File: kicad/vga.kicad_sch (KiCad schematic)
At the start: 5 parts, among them J10 DE15, U20 XC95108PC84

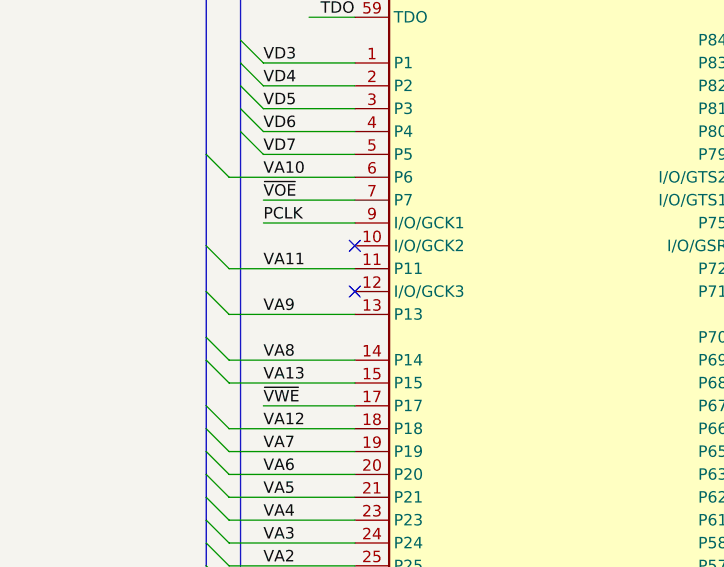
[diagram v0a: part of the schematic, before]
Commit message: hw: add missing shload_n connection
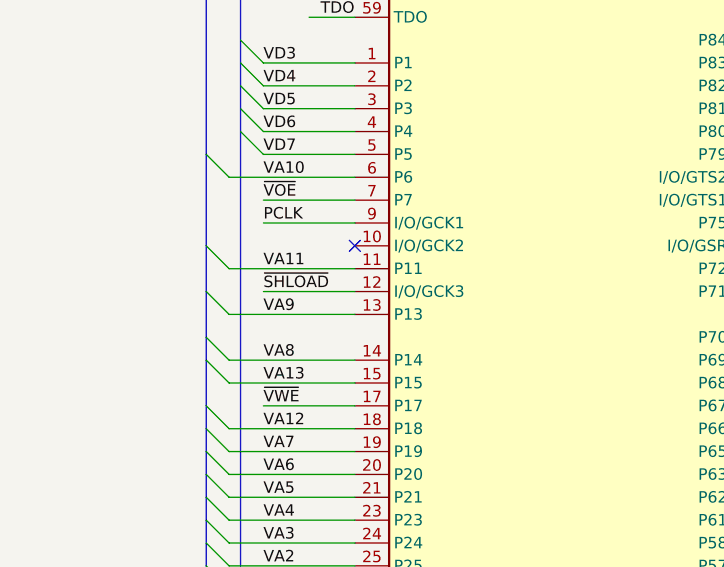
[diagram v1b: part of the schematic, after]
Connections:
- net ~{SHLOAD}: now also U20.12 (I/O/GCK3)
- no-connect marks 11 -> 10
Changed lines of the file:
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@@
 		(title "VGA")
 		(date "2025-06-18")
-		(rev "A")
+		(rev "B")
 		(company "A.K.")
 	)
@@
 	)
 	(no_connect
-		(at 102.87 102.87)
-	)
-	(no_connect
 		(at 250.19 85.09)
 	)
@@
 		(pts
 			(xy 123.19 58.42) (xy 120.65 58.42)
+		)
+		(stroke
+			(width 0)
+			(type default)
+		)
+	)
+	(wire
+		(pts
+			(xy 92.71 102.87) (xy 102.87 102.87)
 		)
 		(stroke
@@
 		)
 	)
+	(label "~{SHLOAD}"
+		(at 92.71 102.87 0)
+		(effects
+			(font
+				(size 1.27 1.27)
+			)
+			(justify left bottom)
+		)
+	)

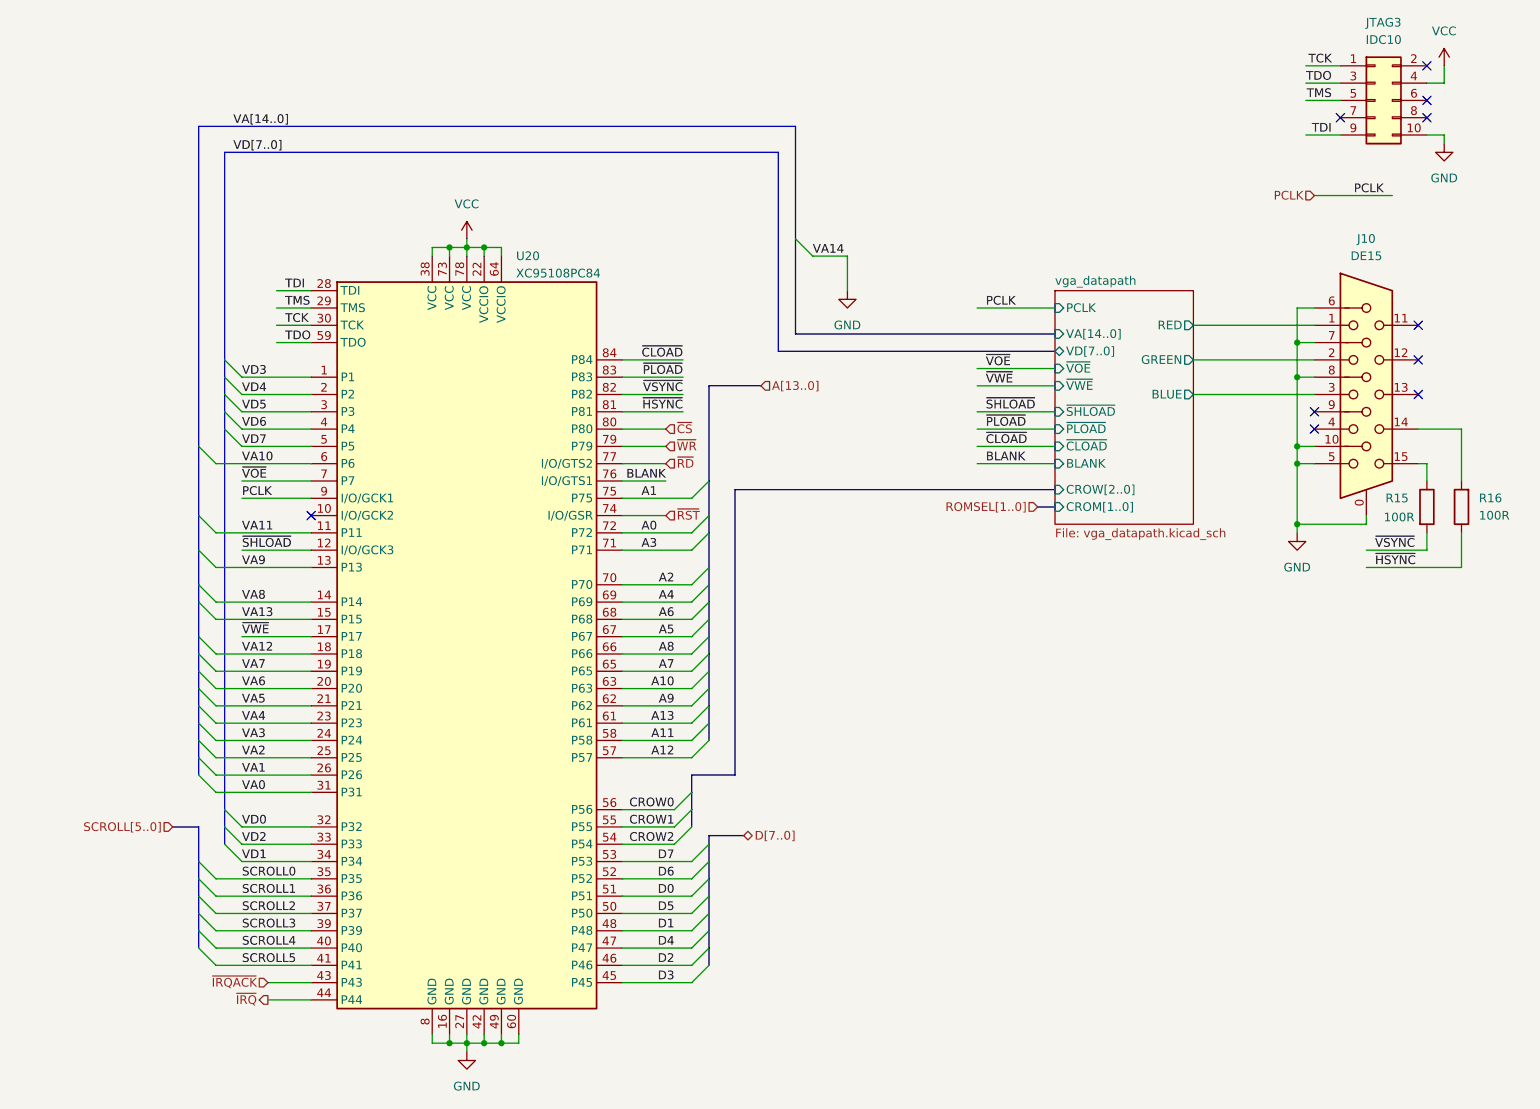
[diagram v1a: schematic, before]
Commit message: hw: replace CPLD JTAG connector, minor fixes
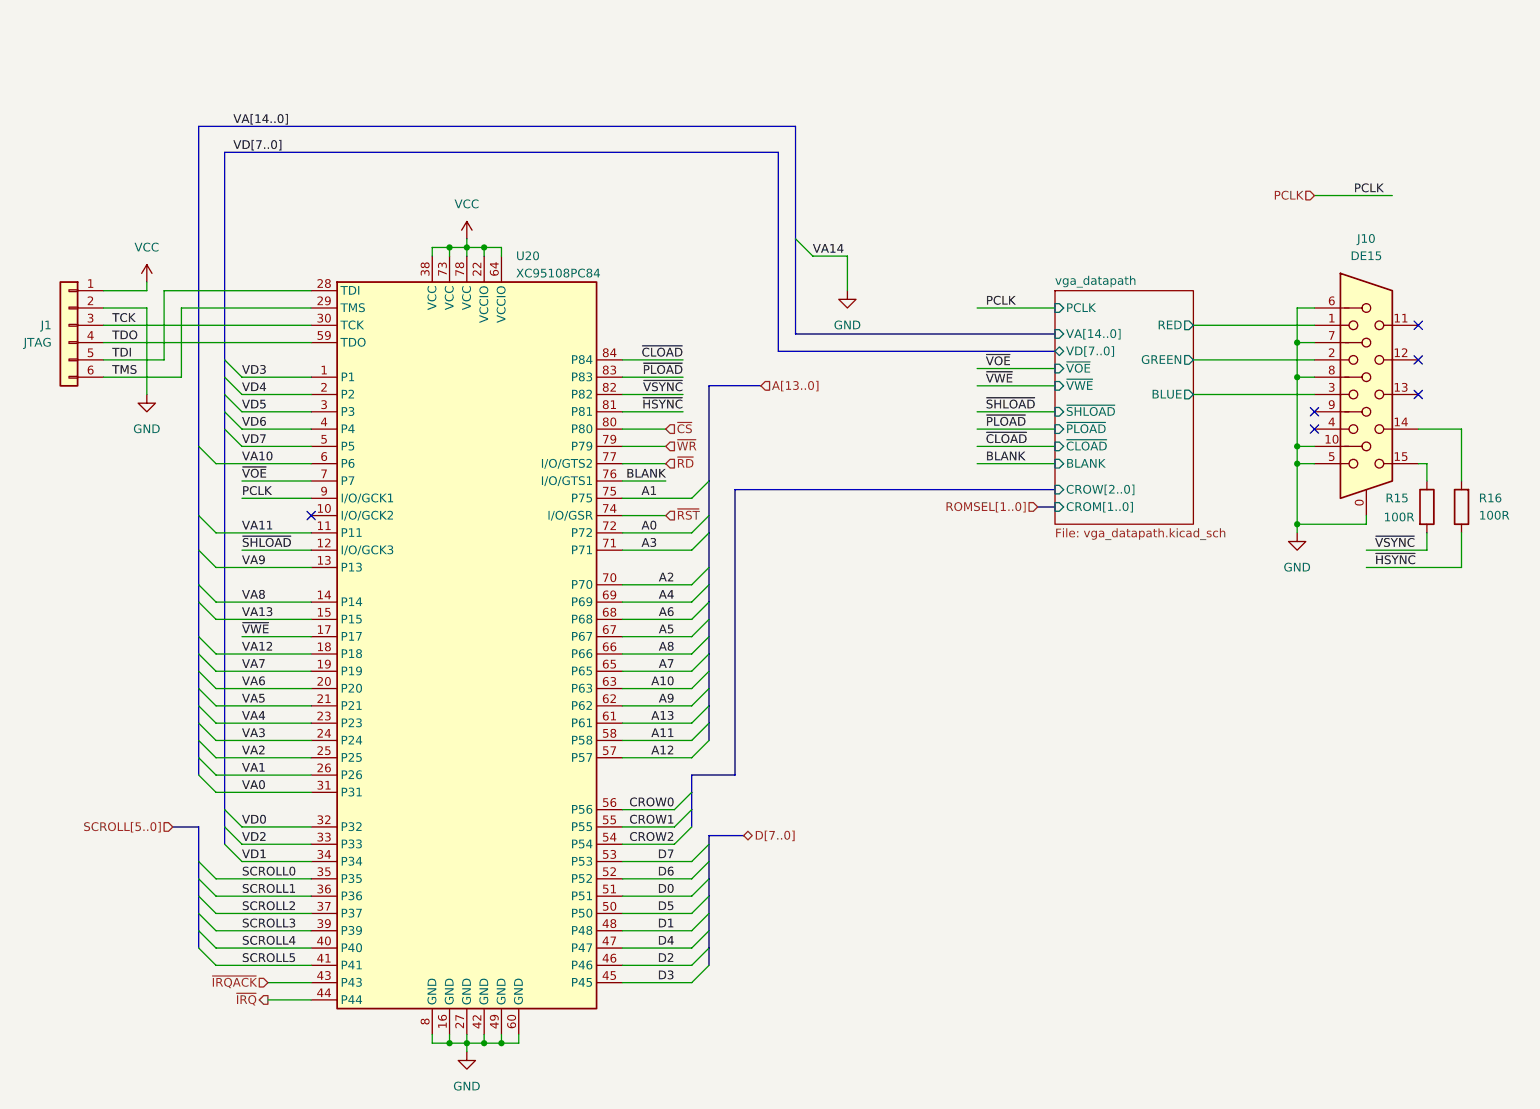
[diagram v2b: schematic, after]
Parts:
- removed JTAG3: IDC10, Connector_IDC:IDC-Header_2x05_P2.54mm_Vertical, symbol Connector_Generic:Conn_02x05_Odd_Even
- added J1: JTAG, Connector_PinHeader_2.54mm:PinHeader_1x06_P2.54mm_Vertical, symbol Connector_Generic:Conn_01x06
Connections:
- net GND: now also J1.2 (Pin_2)
- net TCK: now also J1.3 (Pin_3)
- net TDI: now also J1.5 (Pin_5)
- net TDO: now also J1.4 (Pin_4)
- net TMS: now also J1.6 (Pin_6)
- net VCC: now also J1.1 (Pin_1)
- no-connect marks 10 -> 6

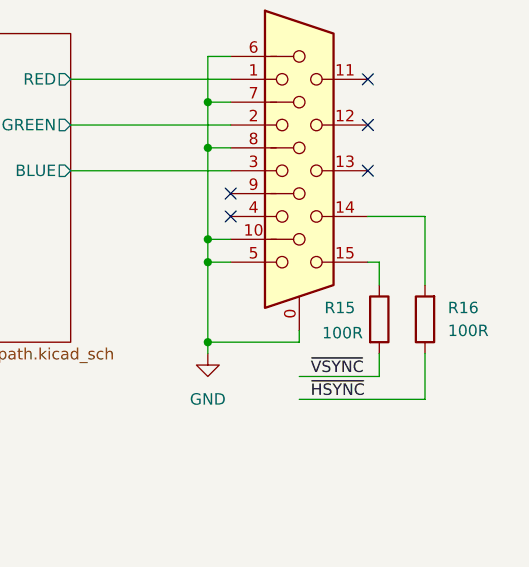
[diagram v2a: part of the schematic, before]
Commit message: hw: fix hsync/vsync being connected to wrong pins
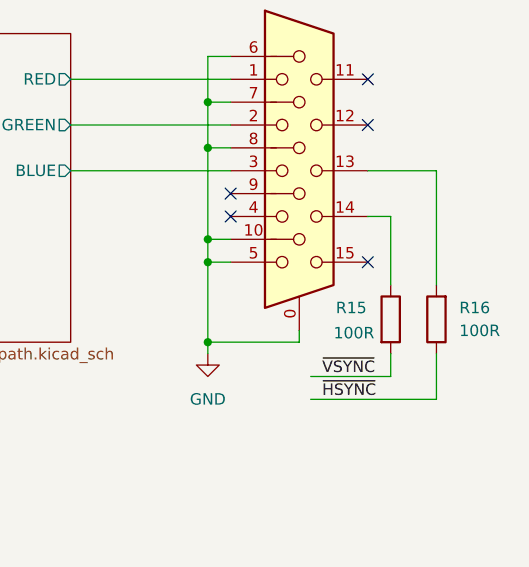
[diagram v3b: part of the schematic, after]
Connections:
- net at R16.2: now also J10.13; no longer J10.14
- net at R15.1: now also J10.14; no longer J10.15
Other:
- moved on the sheet: R15, R16
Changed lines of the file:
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@@
 	)
 	(no_connect
+		(at 265.43 90.17)
+	)
+	(no_connect
 		(at 250.19 82.55)
 	)
@@
 	)
 	(no_connect
-		(at 265.43 80.01)
-	)
-	(no_connect
 		(at 265.43 69.85)
 	)
@@
 	(wire
 		(pts
-			(xy 266.7 92.71) (xy 266.7 90.17)
-		)
-		(stroke
-			(width 0)
-			(type default)
-		)
-	)
-	(wire
-		(pts
 			(xy 92.71 87.63) (xy 102.87 87.63)
 		)
@@
 	(wire
 		(pts
-			(xy 266.7 90.17) (xy 265.43 90.17)
-		)
-		(stroke
-			(width 0)
-			(type default)
-		)
-	)
-	(wire
-		(pts
 			(xy 125.73 175.26) (xy 125.73 176.53)
 		)
@@
 	(wire
 		(pts
-			(xy 148.59 115.57) (xy 158.75 115.57)
+			(xy 273.05 92.71) (xy 273.05 80.01)
 		)
 		(stroke
@@
 	(wire
 		(pts
-			(xy 271.78 85.09) (xy 271.78 92.71)
+			(xy 148.59 115.57) (xy 158.75 115.57)
 		)
 		(stroke
@@
 	(wire
 		(pts
-			(xy 257.81 102.87) (xy 266.7 102.87)
+			(xy 259.08 102.87) (xy 267.97 102.87)
 		)
 		(stroke
@@
 	(wire
 		(pts
-			(xy 257.81 105.41) (xy 271.78 105.41)
+			(xy 259.08 105.41) (xy 273.05 105.41)
 		)
 		(stroke
@@
 	(wire
 		(pts
-			(xy 130.81 175.26) (xy 130.81 173.99)
+			(xy 273.05 80.01) (xy 265.43 80.01)
 		)
 		(stroke
@@
 	(wire
 		(pts
-			(xy 148.59 130.81) (xy 158.75 130.81)
+			(xy 130.81 175.26) (xy 130.81 173.99)
 		)
 		(stroke
@@
 	(wire
 		(pts
-			(xy 265.43 85.09) (xy 271.78 85.09)
+			(xy 148.59 130.81) (xy 158.75 130.81)
 		)
 		(stroke
@@
 	(wire
 		(pts
-			(xy 271.78 105.41) (xy 271.78 100.33)
+			(xy 273.05 105.41) (xy 273.05 100.33)
 		)
 		(stroke
@@
 	(wire
 		(pts
-			(xy 266.7 100.33) (xy 266.7 102.87)
+			(xy 267.97 100.33) (xy 267.97 102.87)
 		)
 		(stroke
@@
 		)
 	)
+	(wire
+		(pts
+			(xy 267.97 92.71) (xy 267.97 85.09)
+		)
+		(stroke
+			(width 0)
+			(type default)
+		)
+	)
 	(bus
 		(pts
@@
 	(wire
 		(pts
+			(xy 267.97 85.09) (xy 265.43 85.09)
+		)
+		(stroke
+			(width 0)
+			(type default)
+		)
+	)
+	(wire
+		(pts
 			(xy 125.73 173.99) (xy 125.73 175.26)
 		)
@@
 	)
 	(label "~{HSYNC}"
-		(at 259.08 105.41 0)
+		(at 260.35 105.41 0)
 		(effects
 			(font
@@
 	)
 	(label "~{VSYNC}"
-		(at 259.08 102.87 0)
+		(at 260.35 102.87 0)
 		(effects
 			(font
@@
 	(symbol
 		(lib_id "Device:R")
-		(at 271.78 96.52 180)
+		(at 273.05 96.52 180)
 		(unit 1)
 		(exclude_from_sim no)
@@
 		(fields_autoplaced yes)
 		(property "Reference" "R16"
-			(at 274.32 95.2499 0)
+			(at 275.59 95.2499 0)
 			(effects
 				(font
@@
 		)
 		(property "Value" "100R"
-			(at 274.32 97.7899 0)
+			(at 275.59 97.7899 0)
 			(effects
 				(font
@@
 		)
 		(property "Footprint" "Resistor_THT:R_Axial_DIN0207_L6.3mm_D2.5mm_P7.62mm_Horizontal"
-			(at 273.558 96.52 90)
+			(at 274.828 96.52 90)
 			(effects
 				(font
@@
 		)
 		(property "Datasheet" "~"
-			(at 271.78 96.52 0)
+			(at 273.05 96.52 0)
 			(effects
 				(font
@@
 		)
 		(property "Description" ""
-			(at 271.78 96.52 0)
+			(at 273.05 96.52 0)
 			(effects
 				(font
@@
 	(symbol
 		(lib_id "Device:R")
-		(at 266.7 96.52 0)
+		(at 267.97 96.52 0)
 		(unit 1)
 		(exclude_from_sim no)
@@
 		(dnp no)
 		(property "Reference" "R15"
-			(at 260.604 95.25 0)
+			(at 261.874 95.25 0)
 			(effects
 				(font
@@
 		)
 		(property "Value" "100R"
-			(at 260.35 98.044 0)
+			(at 261.62 98.044 0)
 			(effects
 				(font
@@
 		)
 		(property "Footprint" "Resistor_THT:R_Axial_DIN0207_L6.3mm_D2.5mm_P7.62mm_Horizontal"
-			(at 264.922 96.52 90)
+			(at 266.192 96.52 90)
 			(effects
 				(font
@@
 		)
 		(property "Datasheet" "~"
-			(at 266.7 96.52 0)
+			(at 267.97 96.52 0)
 			(effects
 				(font
@@
 		)
 		(property "Description" ""
-			(at 266.7 96.52 0)
+			(at 267.97 96.52 0)
 			(effects
 				(font
